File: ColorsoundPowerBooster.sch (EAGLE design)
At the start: 58 parts, among them IC1 MAX1044, Q1 BC169, Q2 BC184, Q3 BC109

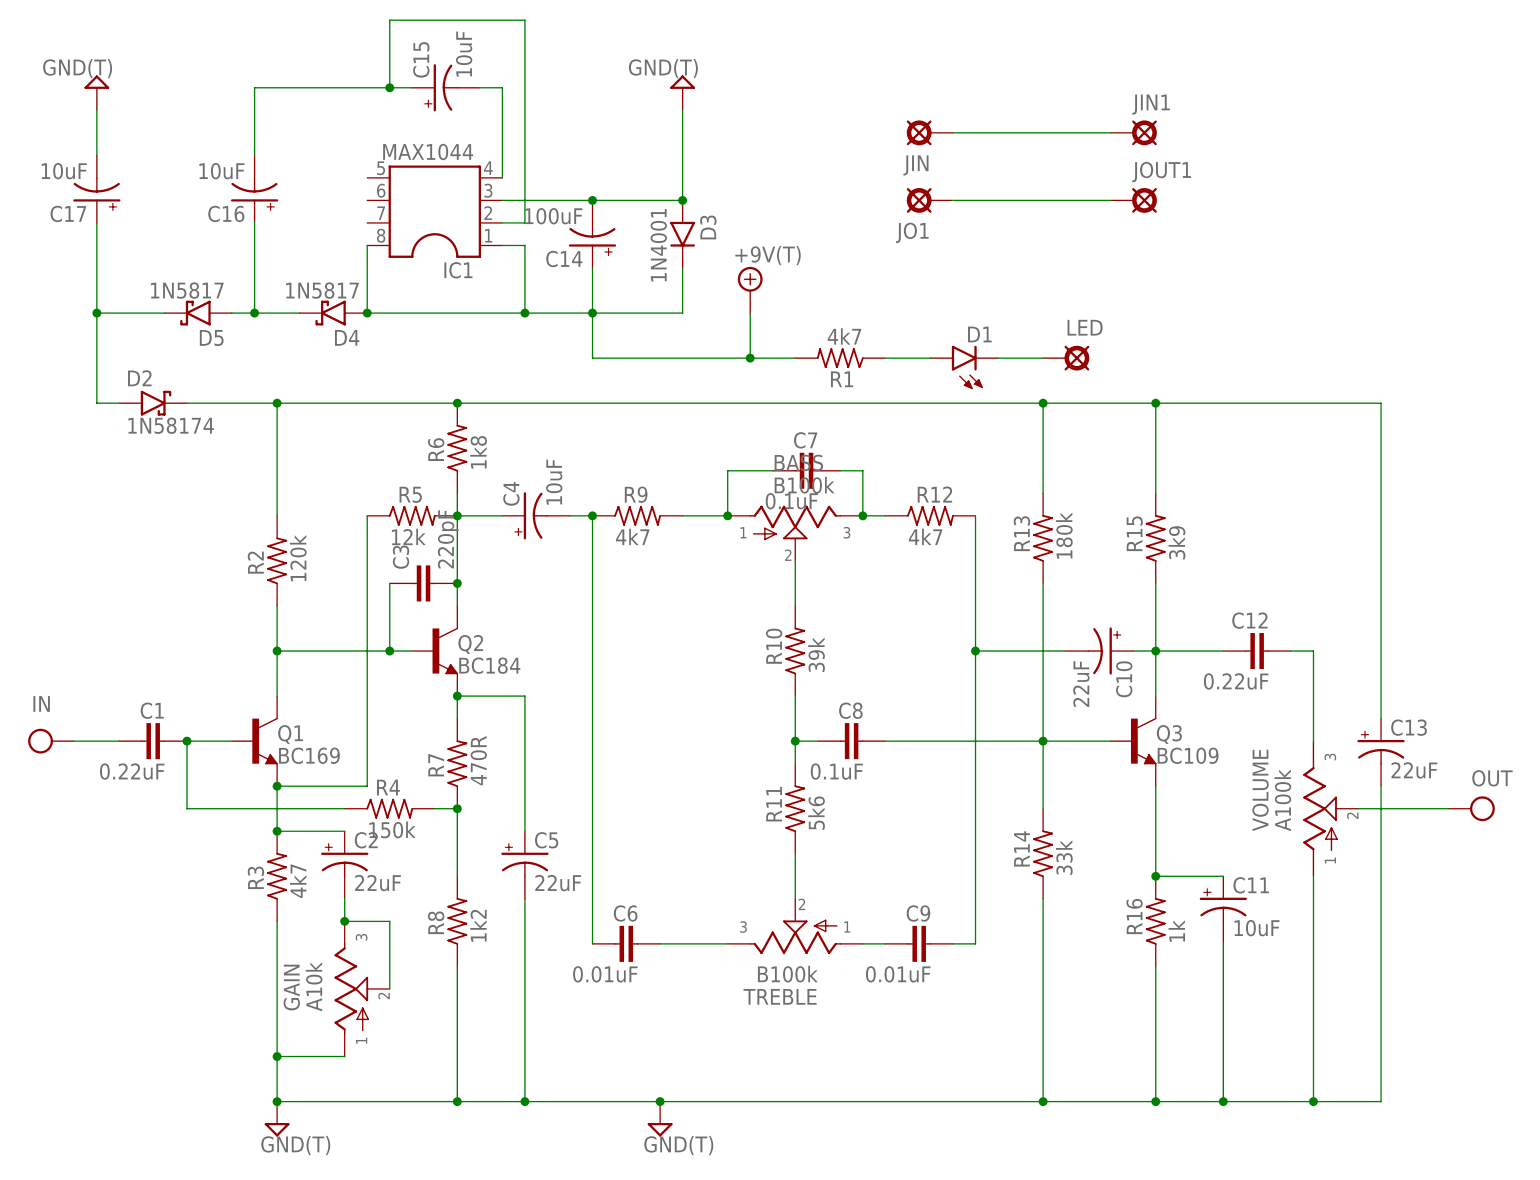
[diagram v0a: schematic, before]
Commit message: Updated to Version 1.1 to fix Gain and Bass pot wire inversion
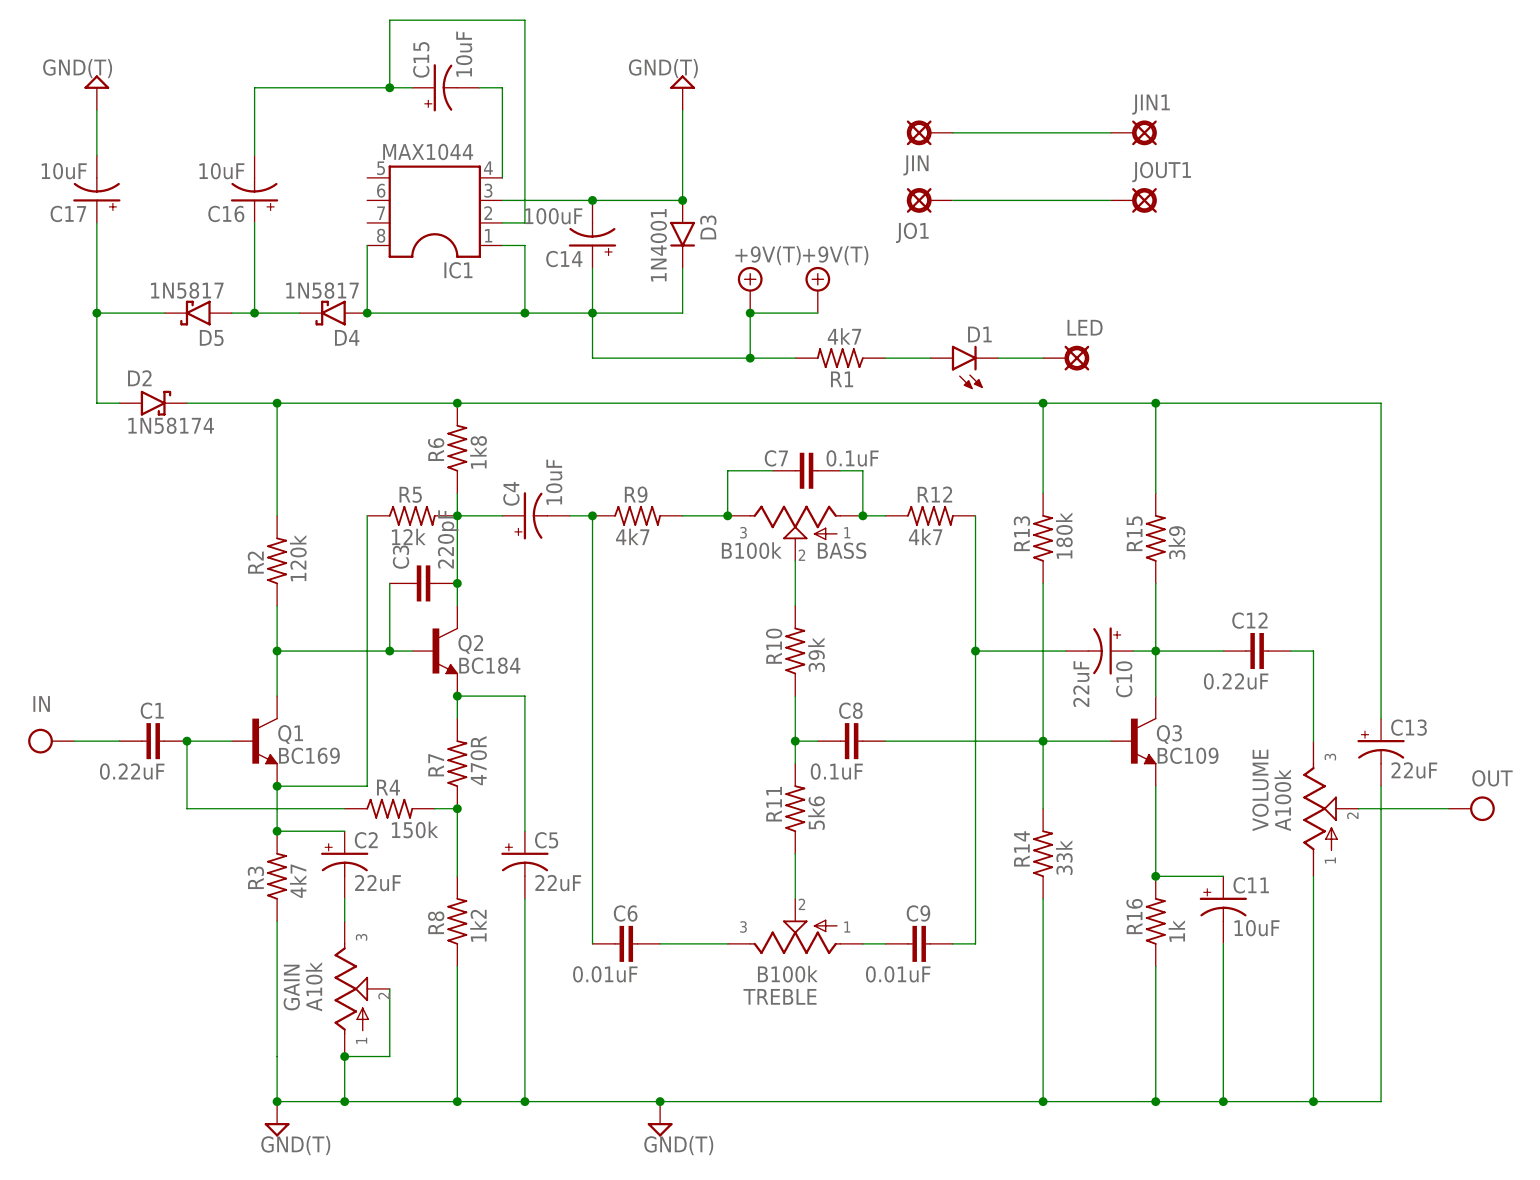
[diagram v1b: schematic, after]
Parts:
- added +9V1: +9V(T), mb_supply:+9V(T)
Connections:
- removed net N$14: BASS.1, C7.1, R9.2
- removed net N$15: BASS.3, C7.2, R12.1
- new net N$30: BASS.3, C7.1, R9.2
- new net N$31: BASS.1, C7.2, R12.1
- net +9V: now also +9V1.+9V
- net GND: now also GAIN.2
- net N$5: no longer GAIN.2
